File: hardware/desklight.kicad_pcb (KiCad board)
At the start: 2 copper layers, 25 x 25 mm, 16 parts, among them IC1 ATTINY10-TS, P1 AVR_TPI, P2 Pwr5V1500mA, P3 WS2812_CON, SW1 Rotary_Encoder_Switch

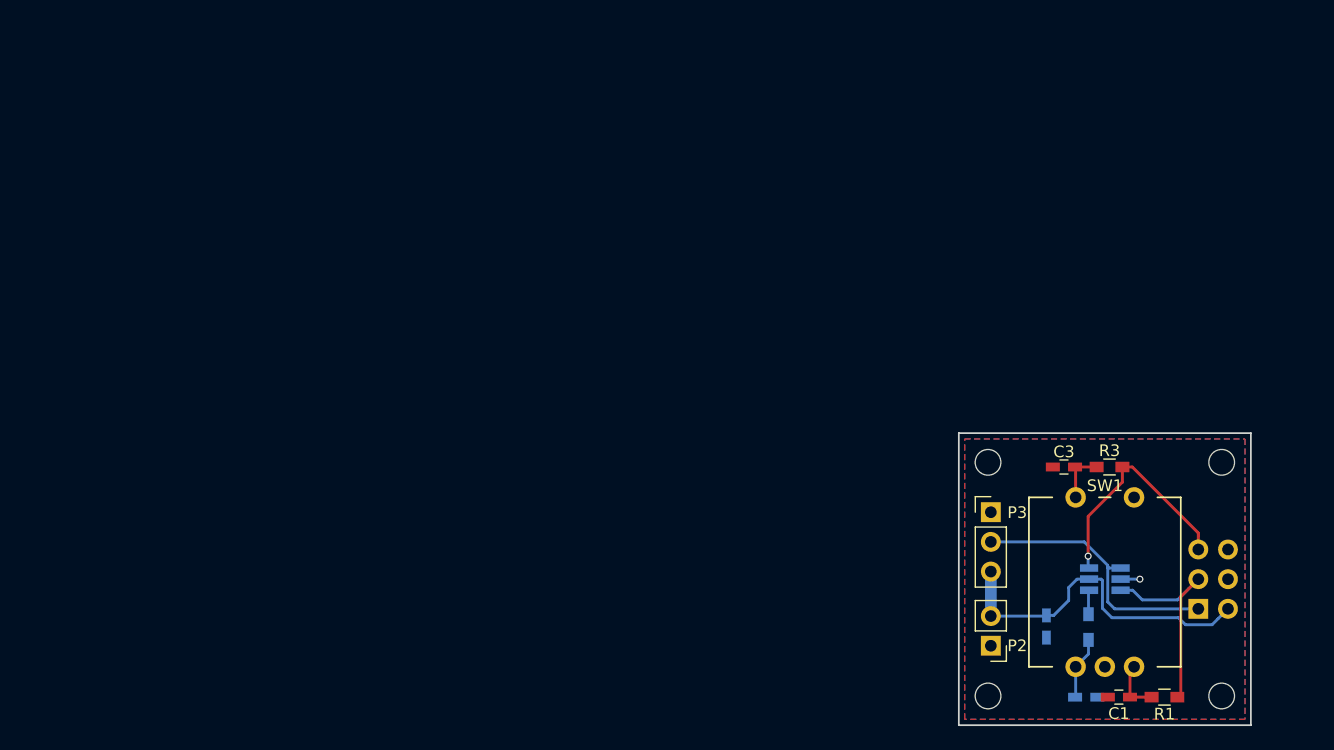
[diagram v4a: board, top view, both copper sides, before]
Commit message: PCB version 1.0, also panelized in 10x10cm and production-ready zip file for upload to your favourite PCB store.
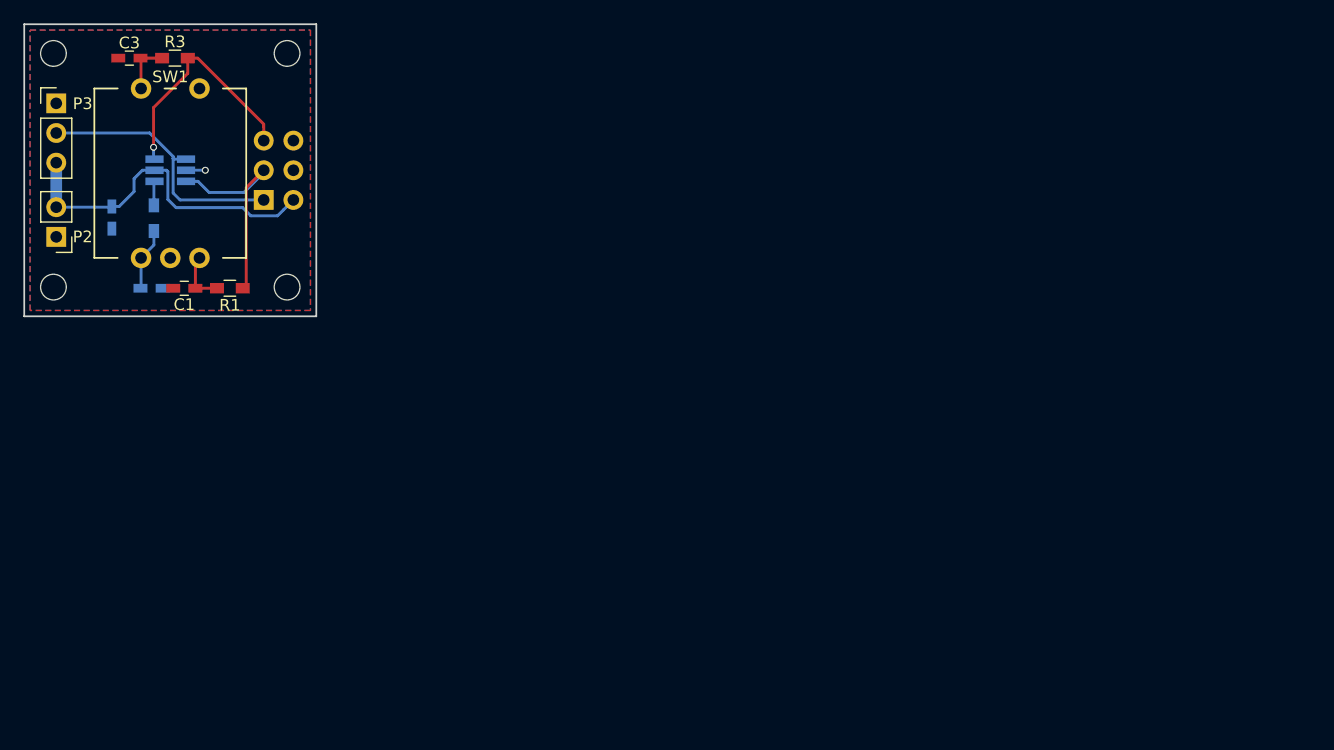
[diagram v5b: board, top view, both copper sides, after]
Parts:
- moved C2 87.3 mm to (60.9, 72.6)
- moved C3 87.3 mm to (59.0, 52.9)
- moved C4 87.3 mm to (57.5, 66.5)
- moved IC1 87.3 mm to (62.5, 62.5)
- moved P1 87.3 mm to (70.5, 65.0)
- moved P2 87.3 mm to (52.7, 68.2)
- moved P3 87.3 mm to (52.7, 56.8)
- moved R1 87.3 mm to (67.6, 72.6)
- moved R2 87.3 mm to (61.1, 66.6)
- moved R3 87.3 mm to (62.9, 52.9)
- moved REF** 87.3 mm to (52.5, 72.5)
- moved REF** 87.3 mm to (72.5, 72.5)
- moved REF** 87.3 mm to (52.5, 52.5)
- moved REF** 87.3 mm to (72.5, 52.5)
- moved SW1 87.3 mm to (62.5, 62.5)
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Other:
- board text added: "github.com/dpiegdon/ tiny-ws2812-desklight v1.0"

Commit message: forward-port PCB to current kicad, include EC11 step model
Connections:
- net /~RESET renamed /~{RESET}
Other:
- net class Default removed
